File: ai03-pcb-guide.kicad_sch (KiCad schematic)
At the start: 14 parts, among them SW1 SW_Push, U2 ATmega32U4-A, Y1 16Mhz

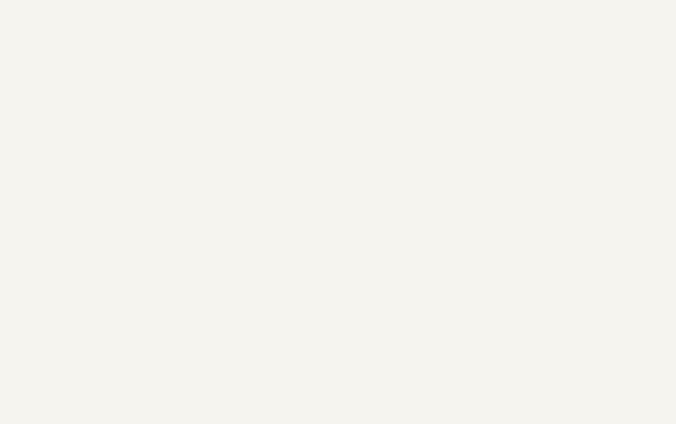
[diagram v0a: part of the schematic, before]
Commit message: Add usb to schematic
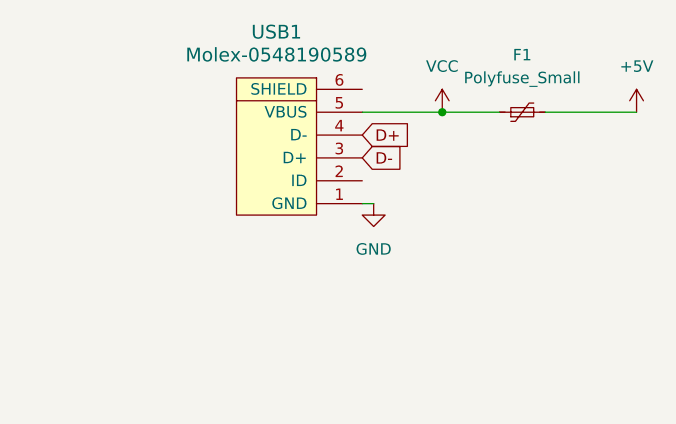
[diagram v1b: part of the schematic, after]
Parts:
- added F1: Polyfuse_Small, symbol Device:Polyfuse_Small
- added USB1: Molex-0548190589, symbol random-keyboard-parts:Molex-0548190589
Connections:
- net +5V: now also F1.2
- net D+: now also USB1.4 (D-)
- net D-: now also USB1.3 (D+)
- net GND: now also USB1.1 (GND)
- new net VCC: F1.1, USB1.5 (VBUS)
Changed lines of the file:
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@@
   (junction (at 81.28 129.54) (diameter 0) (color 0 0 0 0)
   )
+  (junction (at 200.66 54.61) (diameter 0) (color 0 0 0 0)
+  )
   (junction (at 76.2 129.54) (diameter 0) (color 0 0 0 0)
   )
@@
     (stroke (width 0) (type default))
   )
+  (wire (pts (xy 200.66 54.61) (xy 207.01 54.61))
+    (stroke (width 0) (type default))
+  )
   (wire (pts (xy 71.12 83.82) (xy 71.12 87.63))
     (stroke (width 0) (type default))
@@
     (stroke (width 0) (type default))
   )
+  (wire (pts (xy 191.77 54.61) (xy 200.66 54.61))
+    (stroke (width 0) (type default))
+  )
   (wire (pts (xy 71.12 129.54) (xy 76.2 129.54))
     (stroke (width 0) (type default))
@@
     (stroke (width 0) (type default))
   )
+  (wire (pts (xy 212.09 54.61) (xy 222.25 54.61))
+    (stroke (width 0) (type default))
+  )
   (wire (pts (xy 71.12 73.66) (xy 71.12 83.82))
     (stroke (width 0) (type default))
@@
     (stroke (width 0) (type default))
   )
+  (wire (pts (xy 191.77 64.77) (xy 193.04 64.77))
+    (stroke (width 0) (type default))
+  )
   (wire (pts (xy 78.74 78.74) (xy 78.74 86.36))
     (stroke (width 0) (type default))
@@
   (wire (pts (xy 81.28 129.54) (xy 91.44 129.54))
     (stroke (width 0) (type default))
+  )
+  (global_label "D-" (shape input) (at 191.77 59.69 0) (fields_autoplaced)
+    (effects (font (size 1.27 1.27)) (justify left))
+    (property "Intersheetrefs" "${INTERSHEET_REFS}" (at 197.5182 59.69 0)
+      (effects (font (size 1.27 1.27)) (justify left) hide)
+    )
   )
   (global_label "D+" (shape input) (at 68.58 96.52 180) (fields_autoplaced)
@@
     )
   )
+  (global_label "D+" (shape input) (at 191.77 57.15 0) (fields_autoplaced)
+    (effects (font (size 1.27 1.27)) (justify left))
+    (property "Intersheetrefs" "${INTERSHEET_REFS}" (at 197.5182 57.15 0)
+      (effects (font (size 1.27 1.27)) (justify left) hide)
+    )
+  )
   (global_label "D-" (shape input) (at 68.58 99.06 180) (fields_autoplaced)
     (effects (font (size 1.27 1.27)) (justify right))
@@
     )
   )
+  (symbol (lib_id "power:GND") (at 193.04 64.77 0) (unit 1)
+    (in_bom yes) (on_board yes) (dnp no) (fields_autoplaced)
+    (property "Reference" "#PWR011" (at 193.04 71.12 0)
+      (effects (font (size 1.27 1.27)) hide)
+    )
+    (property "Value" "GND" (at 193.04 69.85 0)
+      (effects (font (size 1.27 1.27)))
+    )
+    (property "Footprint" "" (at 193.04 64.77 0)
+      (effects (font (size 1.27 1.27)) hide)
+    )
+    (property "Datasheet" "" (at 193.04 64.77 0)
+      (effects (font (size 1.27 1.27)) hide)
+    )
+    (pin "1")
+    (instances
+      (project "ai03-pcb-guide"
+        (path "/a84ce13a-9ed3-4b81-aa7e-c66be28dc022"
+          (reference "#PWR011") (unit 1)
+        )
+      )
+    )
+  )
   (symbol (lib_id "Device:R_Small_US") (at 82.55 96.52 90) (unit 1)
     (in_bom yes) (on_board yes) (dnp no) (fields_autoplaced)
@@
     )
   )
+  (symbol (lib_id "random-keyboard-parts:Molex-0548190589") (at 184.15 59.69 90) (unit 1)
+    (in_bom yes) (on_board yes) (dnp no) (fields_autoplaced)
+    (property "Reference" "USB1" (at 182.245 45.72 90)
+      (effects (font (size 1.524 1.524)))
+    )
+    (property "Value" "Molex-0548190589" (at 182.245 48.26 90)
+      (effects (font (size 1.524 1.524)))
+    )
+    (property "Footprint" "" (at 184.15 59.69 0)
+      (effects (font (size 1.524 1.524)) hide)
+    )
+    (property "Datasheet" "" (at 184.15 59.69 0)
+      (effects (font (size 1.524 1.524)) hide)
+    )
+    (pin "1")
+    (pin "2")
+    (pin "3")
+    (pin "4")
+    (pin "5")
+    (pin "6")
+    (instances
+      (project "ai03-pcb-guide"
+        (path "/a84ce13a-9ed3-4b81-aa7e-c66be28dc022"
+          (reference "USB1") (unit 1)
+        )
+      )
+    )
+  )
   (symbol (lib_id "Device:C_Small") (at 88.9 106.68 0) (unit 1)
     (in_bom yes) (on_board yes) (dnp no) (fields_autoplaced)
@@
     )
   )
+  (symbol (lib_id "Device:Polyfuse_Small") (at 209.55 54.61 90) (unit 1)
+    (in_bom yes) (on_board yes) (dnp no) (fields_autoplaced)
+    (property "Reference" "F1" (at 209.55 48.26 90)
+      (effects (font (size 1.27 1.27)))
+    )
+    (property "Value" "Polyfuse_Small" (at 209.55 50.8 90)
+      (effects (font (size 1.27 1.27)))
+    )
+    (property "Footprint" "" (at 214.63 53.34 0)
+      (effects (font (size 1.27 1.27)) (justify left) hide)
+    )
+    (property "Datasheet" "~" (at 209.55 54.61 0)
+      (effects (font (size 1.27 1.27)) hide)
+    )
+    (pin "1")
+    (pin "2")
+    (instances
+      (project "ai03-pcb-guide"
+        (path "/a84ce13a-9ed3-4b81-aa7e-c66be28dc022"
+          (reference "F1") (unit 1)
+        )
+      )
+    )
+  )
   (symbol (lib_id "Device:C_Small") (at 60.96 132.08 0) (unit 1)
     (in_bom yes) (on_board yes) (dnp no) (fields_autoplaced)
@@
         (path "/a84ce13a-9ed3-4b81-aa7e-c66be28dc022"
           (reference "#PWR04") (unit 1)
+        )
+      )
+    )
+  )
+  (symbol (lib_id "power:VCC") (at 200.66 54.61 0) (unit 1)
+    (in_bom yes) (on_board yes) (dnp no) (fields_autoplaced)
+    (property "Reference" "#PWR012" (at 200.66 58.42 0)
+      (effects (font (size 1.27 1.27)) hide)
+    )
+    (property "Value" "VCC" (at 200.66 49.53 0)
+      (effects (font (size 1.27 1.27)))
+    )
+    (property "Footprint" "" (at 200.66 54.61 0)
+      (effects (font (size 1.27 1.27)) hide)
+    )
+    (property "Datasheet" "" (at 200.66 54.61 0)
+      (effects (font (size 1.27 1.27)) hide)
+    )
+    (pin "1")
+    (instances
+      (project "ai03-pcb-guide"
+        (path "/a84ce13a-9ed3-4b81-aa7e-c66be28dc022"
+          (reference "#PWR012") (unit 1)
         )
       )
@@
         )
       )
+    )
+  )
+  (symbol (lib_id "power:+5V") (at 222.25 54.61 0) (unit 1)
+    (in_bom yes) (on_board yes) (dnp no) (fields_autoplaced)
+    (property "Reference" "#PWR013" (at 222.25 58.42 0)
+      (effects (font (size 1.27 1.27)) hide)
+    )
+    (property "Value" "+5V" (at 222.25 49.53 0)
+      (effects (font (size 1.27 1.27)))
+    )
+    (property "Footprint" "" (at 222.25 54.61 0)
+      (effects (font (size 1.27 1.27)) hide)
+    )
+    (property "Datasheet" "" (at 222.25 54.61 0)
+      (effects (font (size 1.27 1.27)) hide)
+    )
+    (pin "1")
+    (instances
+      (project "ai03-pcb-guide"
+        (path "/a84ce13a-9ed3-4b81-aa7e-c66be28dc022"
+          (reference "#PWR013") (unit 1)
+        )
+      )

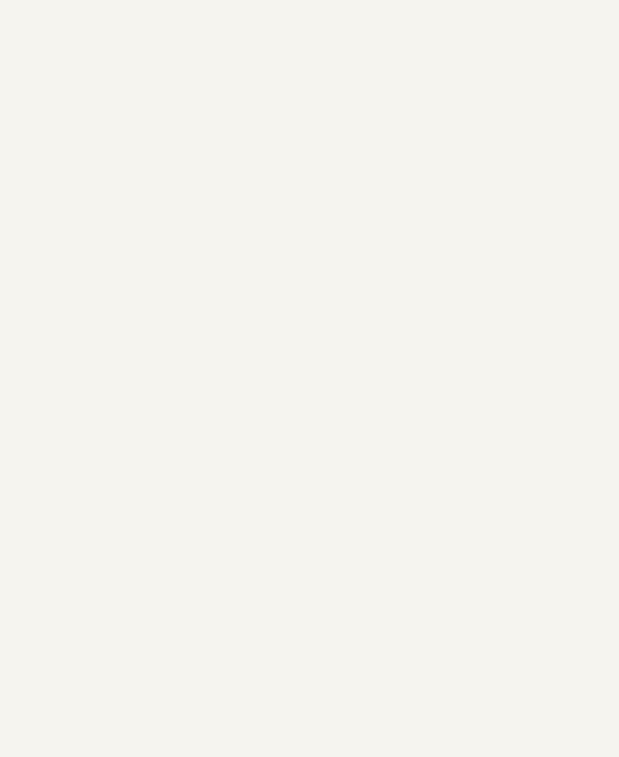
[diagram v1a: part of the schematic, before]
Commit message: Finish matrix and assign footprints
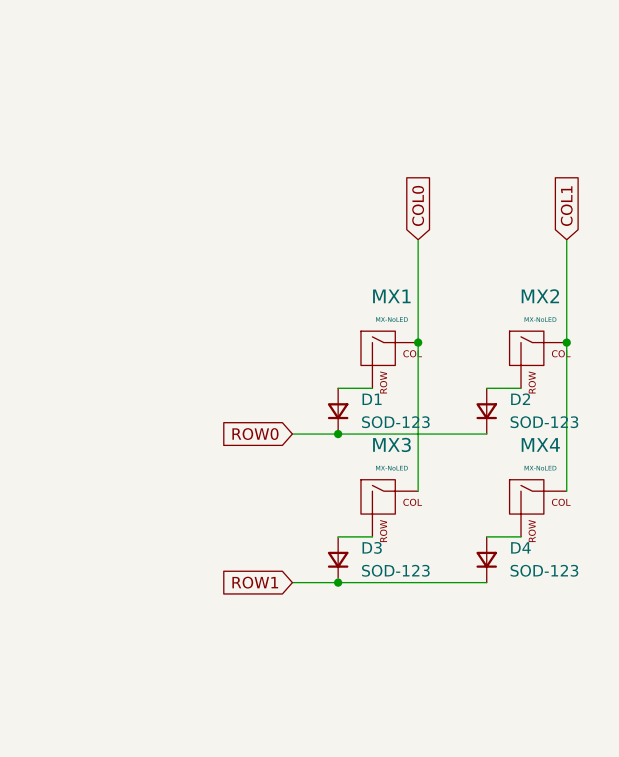
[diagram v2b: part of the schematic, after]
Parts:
- added D1: SOD-123, Diode_SMD:D_SOD-128, symbol Device:D_Small
- added D2, D3, D4: SOD-123, Diode_SMD:D_SOD-123, symbol Device:D_Small
- added MX1, MX2, MX3, MX4: MX-NoLED, MX_Alps_Hybrid:MX-1U-NoLED, symbol MX_Alps_Hybrid:MX-NoLED
- C1, C2, C3, C4, C5, C6, C7: footprint (none) -> Capacitor_SMD:C_0805_2012Metric_Pad1.18x1.45mm_HandSolder
- F1: footprint (none) -> Fuse:Fuse_1206_3216Metric_Pad1.42x1.75mm_HandSolder
- R1, R2, R3, R4: footprint (none) -> Resistor_SMD:R_0805_2012Metric_Pad1.20x1.40mm_HandSolder
- SW1: footprint (none) -> random-keyboard-parts:SKQG-1155865
- USB1: footprint (none) -> random-keyboard-parts:Molex-0548190589
- Y1: footprint (none) -> Crystal:Crystal_SMD_3225-4Pin_3.2x2.5mm_HandSoldering
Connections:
- new net: D4.2 (A), MX4.2 (ROW)
- new net: D2.2 (A), MX2.2 (ROW)
- new net: D1.2 (A), MX1.2 (ROW)
- new net: D3.2 (A), MX3.2 (ROW)
- new net COL0: MX1.1 (COL), MX3.1 (COL)
- new net COL1: MX2.1 (COL), MX4.1 (COL)
- new net ROW0: D1.1 (K), D2.1 (K)
- new net ROW1: D3.1 (K), D4.1 (K)

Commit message: Done routing
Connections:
- net COL0: now also U2.30 (PB6)
- net COL1: now also U2.29 (PB5)
- net ROW0: now also U2.28 (PB4)
- net ROW1: now also U2.31 (PC6)
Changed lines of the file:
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@@
+    )
+  )
+  (global_label "ROW0" (shape input) (at 134.62 81.28 0) (fields_autoplaced)
+    (effects (font (size 1.27 1.27)) (justify left))
+    (property "Intersheetrefs" "${INTERSHEET_REFS}" (at 142.7872 81.28 0)
+      (effects (font (size 1.27 1.27)) (justify left) hide)
     )
   )
@@
     )
   )
+  (global_label "COL0" (shape input) (at 134.62 86.36 0) (fields_autoplaced)
+    (effects (font (size 1.27 1.27)) (justify left))
+    (property "Intersheetrefs" "${INTERSHEET_REFS}" (at 142.3639 86.36 0)
+      (effects (font (size 1.27 1.27)) (justify left) hide)
+    )
+  )
   (global_label "COL0" (shape input) (at 217.17 101.6 90) (fields_autoplaced)
     (effects (font (size 1.27 1.27)) (justify left))
@@
     )
   )
+  (global_label "COL1" (shape input) (at 134.62 83.82 0) (fields_autoplaced)
+    (effects (font (size 1.27 1.27)) (justify left))
+    (property "Intersheetrefs" "${INTERSHEET_REFS}" (at 142.3639 83.82 0)
+      (effects (font (size 1.27 1.27)) (justify left) hide)
+    )
+  )
   (global_label "D-" (shape input) (at 68.58 99.06 180) (fields_autoplaced)
     (effects (font (size 1.27 1.27)) (justify right))
@@
     )
   )
+  (global_label "ROW1" (shape input) (at 134.62 93.98 0) (fields_autoplaced)
+    (effects (font (size 1.27 1.27)) (justify left))
+    (property "Intersheetrefs" "${INTERSHEET_REFS}" (at 142.7872 93.98 0)
+      (effects (font (size 1.27 1.27)) (justify left) hide)
+    )
+  )
